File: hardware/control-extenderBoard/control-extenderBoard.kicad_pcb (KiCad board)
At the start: 4 copper layers, 197.5 x 108.9 mm, 164 parts, among them J1 12V + GND (TP), J10 SCL1 + GND (TP), J11 SDA1 + GND (TP), J12 3V3 + GND (TP), J13 12V + GND (TP), J14 SCL6 + GND (TP), J15 SDA6 + GND (TP), J16 12V + GND (TP), J17 24V IN, J18 GND, J19 3V3 + GND (TP), J2 CAT6-Shield, J20 SCL6 + GND (TP), J21 SDA6 + GND (TP), J22 SDA, SCL - ESP32, J23 I2C7 Reserve SCL/GND, J24 I2C6 Reserve SDA/GND, J25 I2C7 Reserve SDA/GND, J26 I2C6 Reserve SCL/GND, J27 CAT6-Shield, J28 CAT6-Shield, J29 Chassis, J3 Conn_01x02_Pin, J30 RX DIR, J31 TX, GND, J32 12V out, J33 5V out, J34 3V3 out, J35 Conn_01x02_Pin, J36 Conn_01x02_Pin, J37 Conn_01x02_Pin, J38 Conn_01x02_Pin, J39 Conn_01x02_Pin, J4 3V3 + GND (TP), J5 GND, J8 RS485, U1 MAX3485, U10 LM2576T-12, U13 AS5600_Breakout, U14 PCA9600D, U2 PCA9600D, U3 TCA9548A_1-to-8_I2C_Multiplex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, U4 LM2576T-3.3, U8 PCA9600D, U9 LM2576T-5

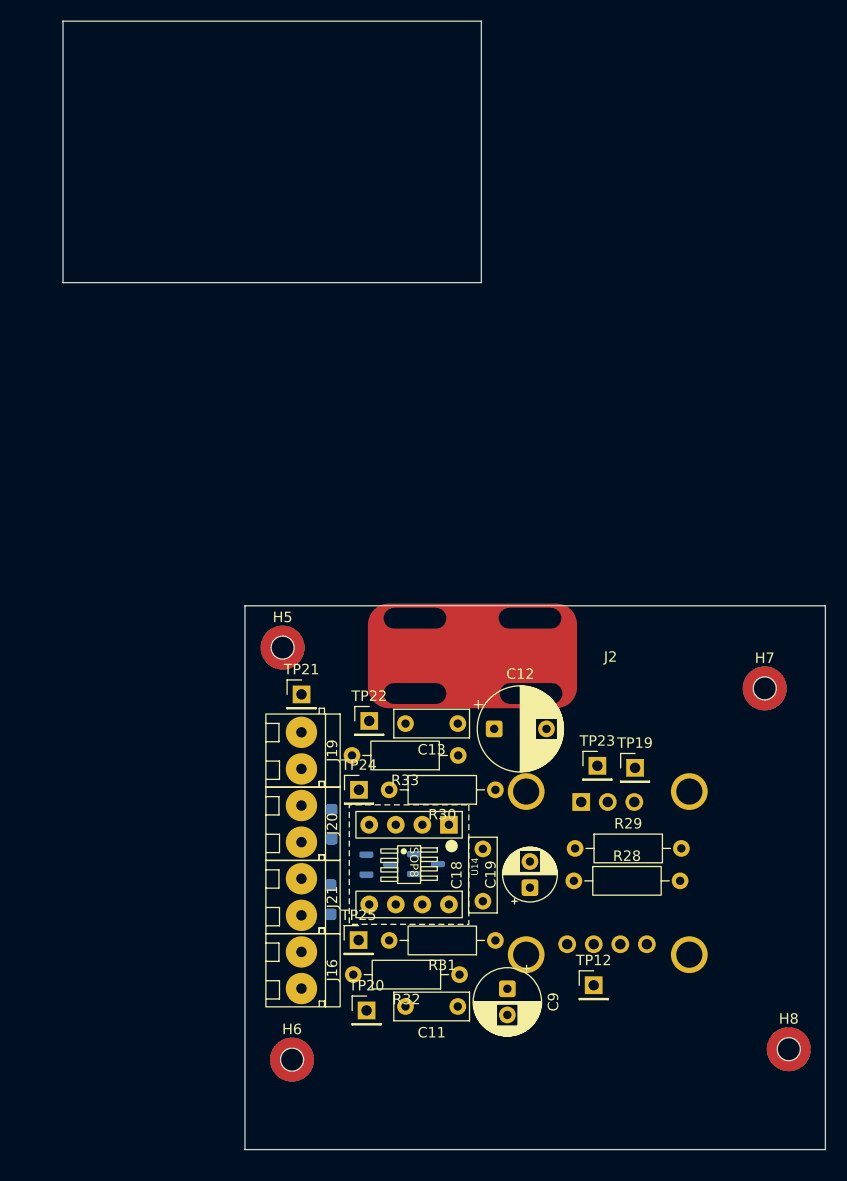
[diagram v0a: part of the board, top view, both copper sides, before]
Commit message: extenderBoard: Route separate remote/sensor-board
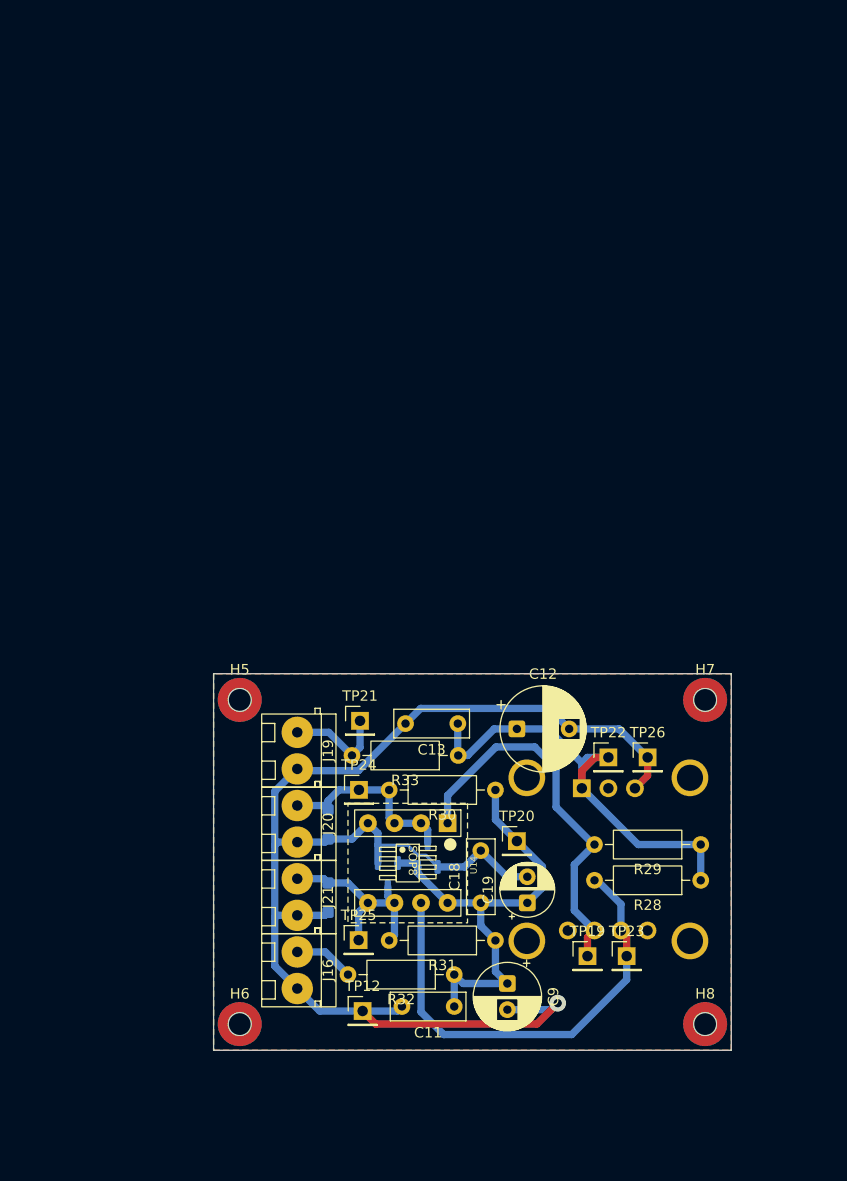
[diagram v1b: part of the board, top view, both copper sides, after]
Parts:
- removed J2: CAT6-Shield, misc_libJonny:Shield_Landing_Pad_6mmCable_ZipTie
- added TP26: GND, Connector_PinHeader_2.54mm:PinHeader_1x01_P2.54mm_Vertical, F.Cu at (225.5, 91.5)
- moved TP22 23.1 mm to (221.8, 91.5)
- moved TP12 22.2 mm to (198.2, 115.8)
- moved TP20 21.7 mm to (213.0, 99.5)
- moved TP19 18.6 mm to (219.8, 110.5)
- moved TP23 18.4 mm to (223.5, 110.5)
- moved R28 12.1 mm to (230.6, 103.2), turned to 180 degrees
- moved R29 12.0 mm to (230.6, 99.8), turned to 180 degrees
- moved H8 8.35 mm to (231.0, 117.0)
- moved H5 6.47 mm to (186.5, 86.0)
- moved TP21 6.14 mm to (198.0, 88.0)
- moved H6 6.05 mm to (186.5, 117.0)
- moved H7 5.81 mm to (231.0, 86.0)
- moved C12 2.17 mm to (213.0, 88.8)
- moved C19 1.48 mm to (214.0, 105.4)
- moved D14 1.34 mm to (200.7, 102.7), turned to -90 degrees
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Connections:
- net Net-(U13-SCL) renamed /Remote-I2C-Sensor-Board/SCL_AS5600
- net Net-(U13-SDA) renamed /Remote-I2C-Sensor-Board/SDA_AS5600
- J20 pad 1: GND_REMOTE -> /Remote-I2C-Sensor-Board/SCL_REMOTE-IN
- J20 pad 2: /Remote-I2C-Sensor-Board/SCL_REMOTE-IN -> GND_REMOTE
- J21 pad 1: GND_REMOTE -> /Remote-I2C-Sensor-Board/SDA_REMOTE-IN
- J21 pad 2: /Remote-I2C-Sensor-Board/SDA_REMOTE-IN -> GND_REMOTE
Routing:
- net GND_REMOTE: track 0.00 -> 136.5 mm, vias 0 -> 1
- net +12V_REMOTE: track 0.00 -> 44.8 mm
- net +3V3_REMOTE: track 0.00 -> 44.2 mm
- net /Remote-I2C-Sensor-Board/SDA_AS5600: track 0.00 -> 44.1 mm
- net /Remote-I2C-Sensor-Board/SCL_AS5600: track 0.00 -> 37.2 mm
- net /Remote-I2C-Sensor-Board/SDA_REMOTE-IN: track 0.00 -> 19.8 mm
- net /Remote-I2C-Sensor-Board/SCL_REMOTE-IN: track 0.00 -> 18.3 mm
- net /Remote-I2C-Sensor-Board/3V3_REMOTE-IN: track 0.00 -> 9.78 mm
- net /Remote-I2C-Sensor-Board/12V_REMOTE-IN: track 0.00 -> 5.75 mm
- added copper zone on B.Cu, net GND_REMOTE
- added copper zone on F.Cu, net GND_REMOTE
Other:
- board size 197.5 x 108.9 mm -> 188.5 x 100 mm
- board text added: "SCL"
- board text added: "SDA"

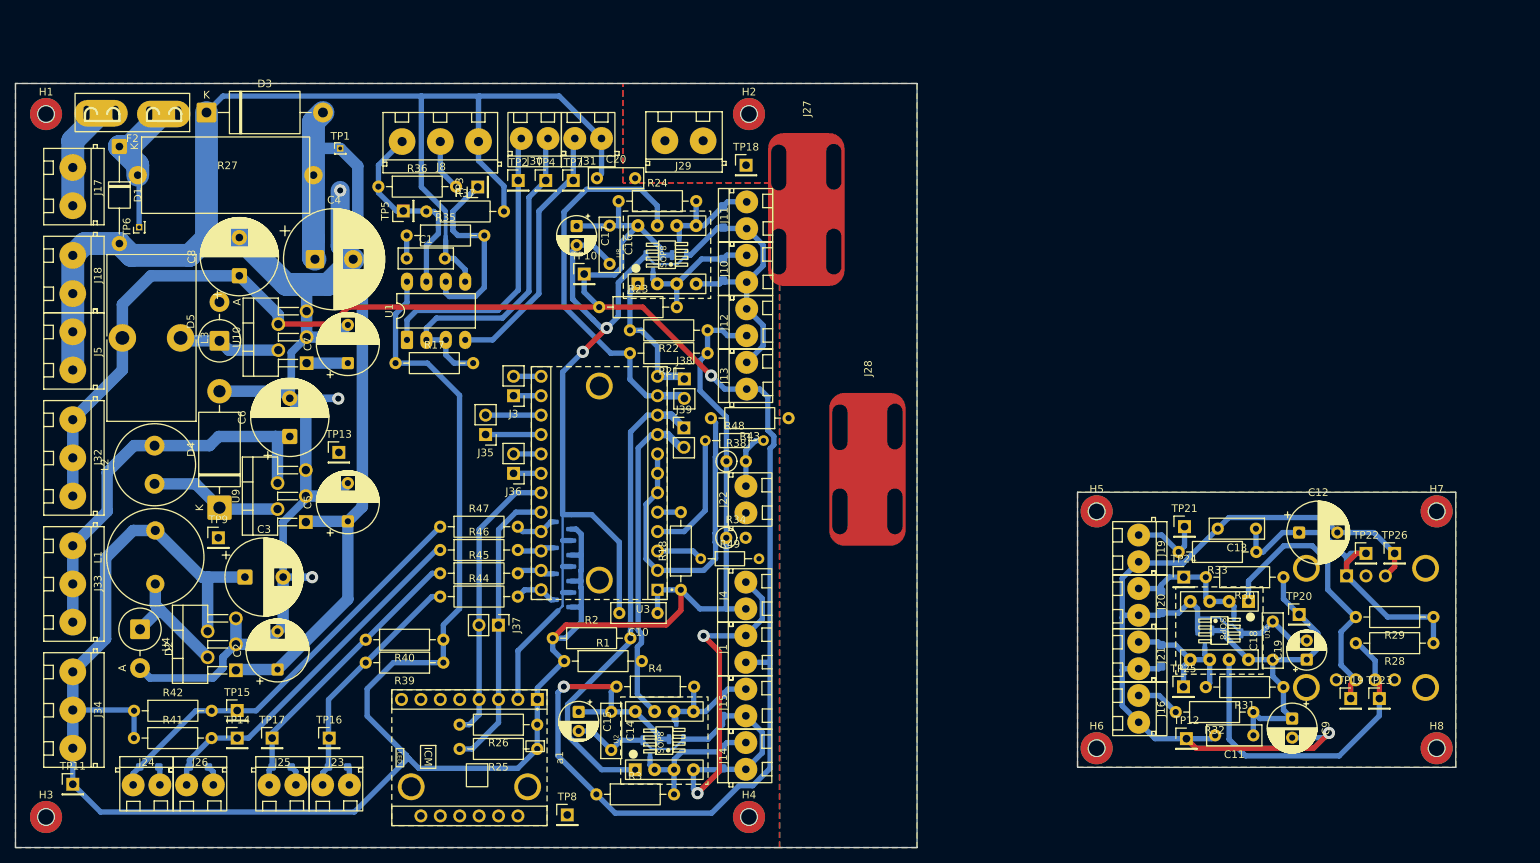
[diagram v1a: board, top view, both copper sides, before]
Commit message: extenderBoard: Add ferrite-beads, Swap 12V TVS diodes
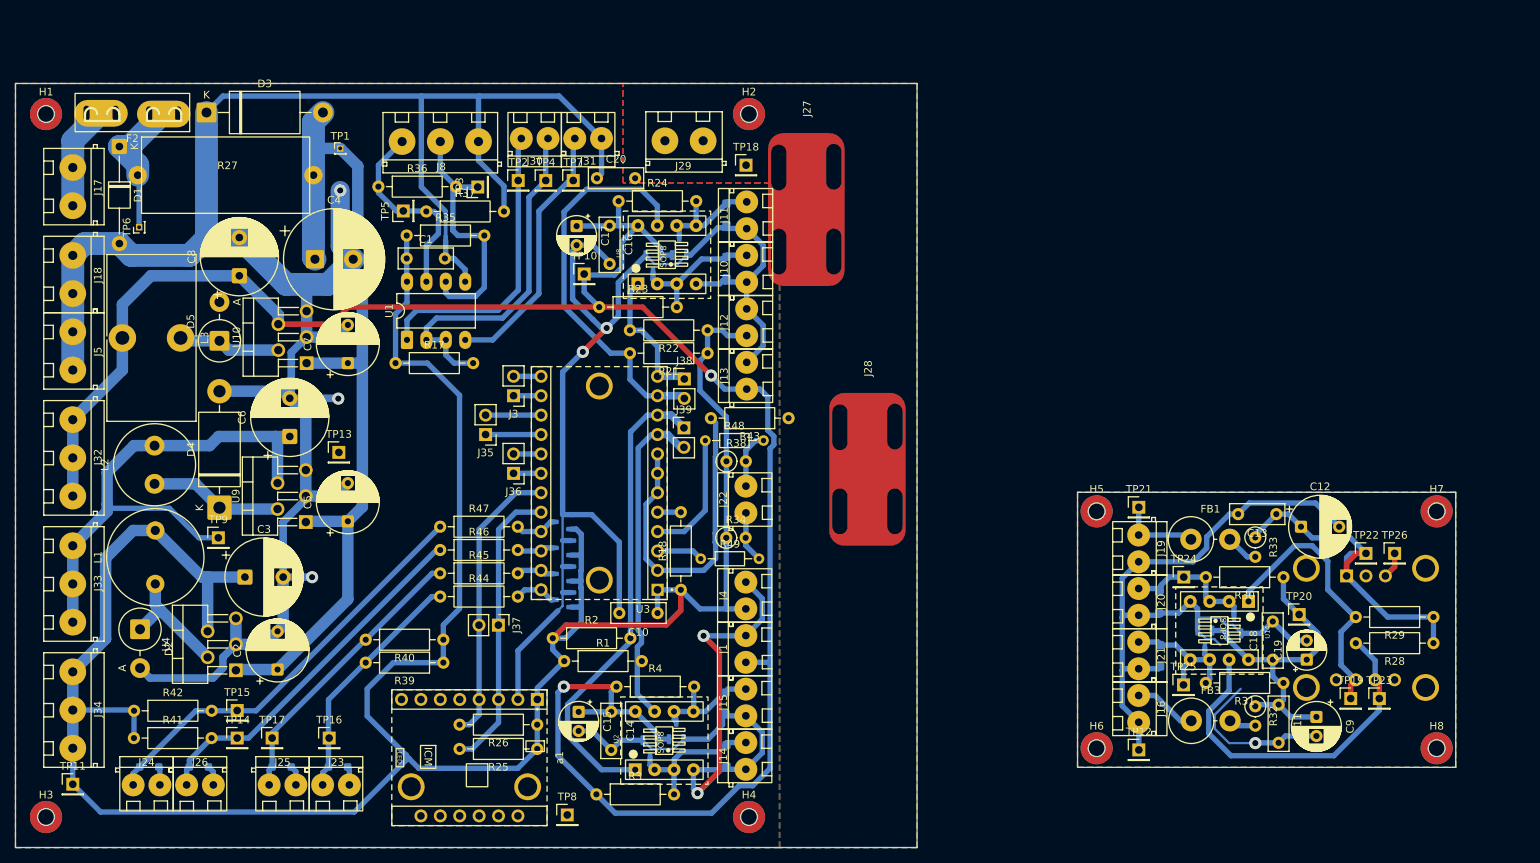
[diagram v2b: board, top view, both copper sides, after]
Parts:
- removed D15: SMF12VTR, Diode_SMD:D_SOD-123F
- added D31: PESD12VL1BA, Diode_SMD:D_SOD-123F, B.Cu at (138.0, 54.1)
- added FB1: FerriteBead AWBC-09, Resistor_THT:R_Axial_DIN0614_L14.3mm_D5.7mm_P5.08mm_Vertical, F.Cu at (198.8, 89.7)
- added FB3: FerriteBead AWBC-09, Resistor_THT:R_Axial_DIN0614_L14.3mm_D5.7mm_P5.08mm_Vertical, F.Cu at (198.9, 113.4)
- D11, D12, D16, D8, D9: value SMF12VTR -> PESD12VL1BA
- R32, R33: footprint Resistor_THT:R_Axial_DIN0207_L6.3mm_D2.5mm_P10.16mm_Horizontal -> Resistor_THT:R_Axial_DIN0207_L6.3mm_D2.5mm_P2.54mm_Vertical
- moved D9 70.5 mm to (138.0, 118.0), turned to 90 degrees
- moved D12 58.8 mm to (194.8, 104.9), turned to 90 degrees
- moved D8 7.27 mm to (138.0, 47.1), turned to 90 degrees
- moved D16 6.99 mm to (194.7, 97.9), turned to 90 degrees
- moved TP21 6.49 mm to (192.0, 85.5)
- moved TP12 6.40 mm to (192.0, 117.2)
- moved C11 5.21 mm to (210.3, 111.3), turned to -90 degrees
- moved C13 3.28 mm to (210.0, 86.4)
- moved C9 3.18 mm to (215.3, 112.9)
- moved R33 1.91 mm to (207.3, 89.4), turned to -90 degrees
- moved R32 0.80 mm to (207.3, 111.5), turned to -90 degrees
- moved C12 0.80 mm to (213.2, 88.0)
- moved R31 0.54 mm to (210.9, 108.5)
- moved D11 0.46 mm to (137.9, 111.1), turned to 90 degrees
- moved TP25 0.25 mm to (197.9, 108.7)
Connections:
- D11 pad 1: /SDA_Boost1 -> GND
- D11 pad 2: GND -> /SDA_Boost1
- D12 pad 1: /SCL_Boost1 -> GND_REMOTE
- D12 pad 2: GND -> /Remote-I2C-Sensor-Board/SDA_REMOTE-IN
- D16 pad 1: /Remote-I2C-Sensor-Board/SDA_REMOTE-IN -> GND_REMOTE
- D16 pad 2: GND_REMOTE -> /Remote-I2C-Sensor-Board/SCL_REMOTE-IN
- D8 pad 1: /SCL_Boost2 -> GND
- D8 pad 2: GND -> /SDA_Boost2
- D9 pad 1: /SDA_Boost2 -> GND
- D9 pad 2: GND -> /SCL_Boost1
- R32 pad 2: /Remote-I2C-Sensor-Board/12V_REMOTE-IN -> Net-(FB3-Pad2)
- R33 pad 2: /Remote-I2C-Sensor-Board/3V3_REMOTE-IN -> Net-(FB1-Pad2)
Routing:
- net +5V: track 53.5 -> 69.9 mm
- net GND_REMOTE: track 136.5 -> 122.4 mm
- net /ESP32_SDA: track 0.00 -> 6.74 mm
- net Net-(FB1-Pad2): track 0.00 -> 4.29 mm
- net Net-(FB3-Pad2): track 0.00 -> 3.57 mm
- net +3V3: track 341.5 -> 344.5 mm
- net /Remote-I2C-Sensor-Board/SDA_AS5600: track 44.1 -> 47.0 mm
- net /Remote-I2C-Sensor-Board/12V_REMOTE-IN: track 5.75 -> 8.25 mm
- net +24V filtered: track 114.8 -> 116.8 mm
- net /RS485-A: track 32.2 -> 33.9 mm
- net +12V_REMOTE: track 44.8 -> 43.4 mm
- net /Remote-I2C-Sensor-Board/3V3_REMOTE-IN: track 9.78 -> 10.7 mm
- net /Remote-I2C-Sensor-Board/SCL_AS5600: track 37.2 -> 36.4 mm
- net /Remote-I2C-Sensor-Board/SDA_REMOTE-IN: track 19.8 -> 19.0 mm
- net +3V3_REMOTE: track 44.2 -> 45.0 mm

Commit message: extenderBoard: Optimize zones, routing, Fix errors - DRC pass
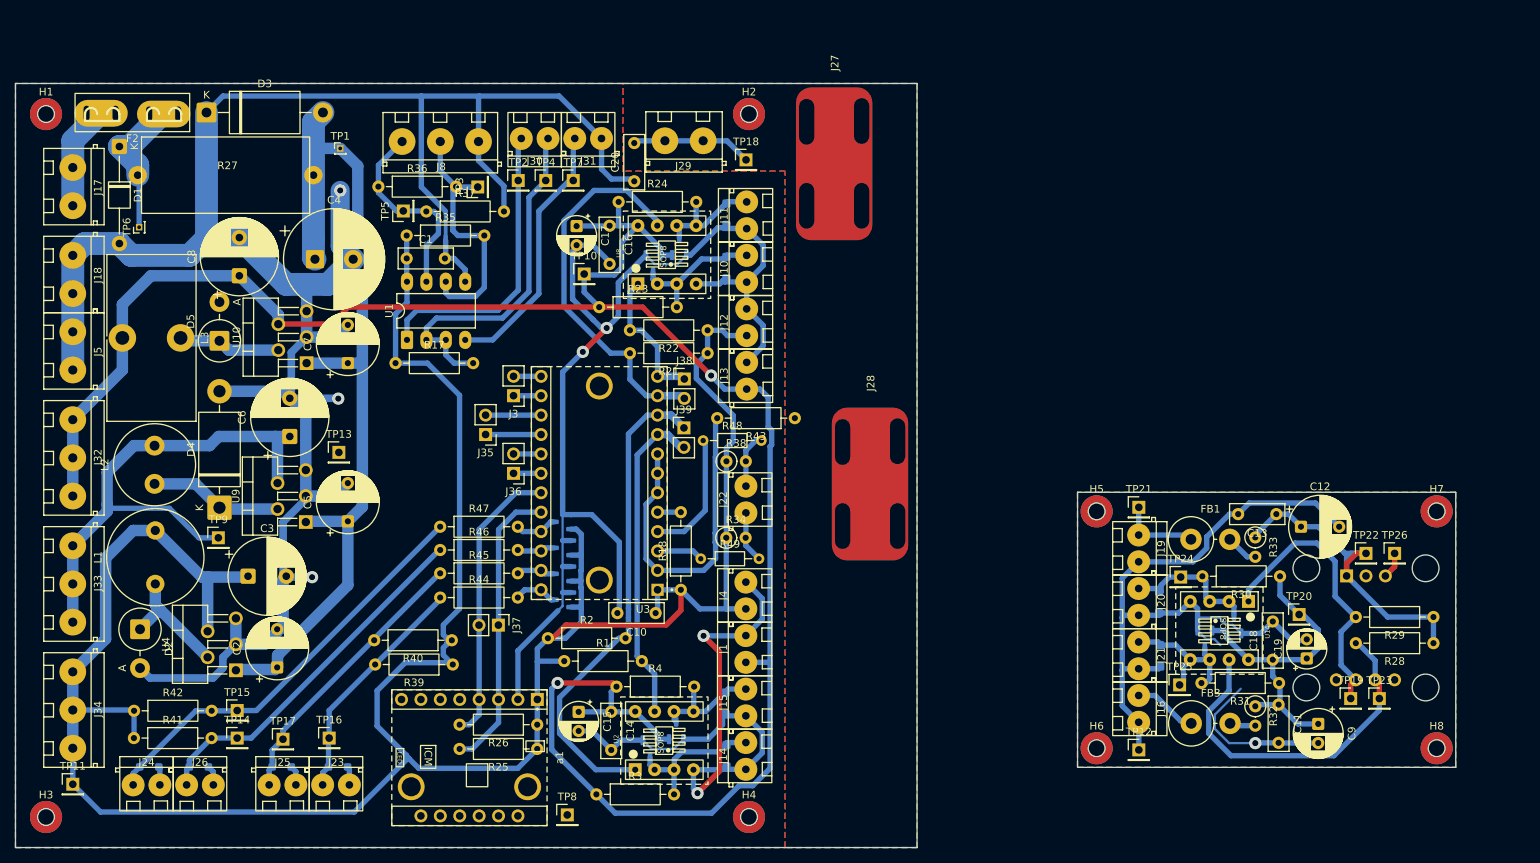
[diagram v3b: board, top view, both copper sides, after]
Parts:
- moved J27 7.01 mm to (152.1, 40.5)
- moved C20 4.90 mm to (126.0, 42.8), turned to 90 degrees
- moved J28 1.95 mm to (156.8, 82.4)
- moved TP17 1.43 mm to (80.0, 115.8)
- moved R39 1.26 mm to (102.2, 106.0)
- moved R40 1.11 mm to (102.1, 102.9)
- moved C9 0.94 mm to (215.5, 113.8)
- moved R43 0.82 mm to (147.0, 73.8)
- moved TP18 0.69 mm to (140.6, 40.0)
- moved R2 0.64 mm to (114.7, 102.6)
- moved R31 0.57 mm to (210.4, 108.5)
- moved TP25 0.51 mm to (197.4, 108.7)
- moved R30 0.46 mm to (210.5, 94.5)
- moved C3 0.42 mm to (75.4, 94.5)
- moved TP24 0.40 mm to (197.5, 94.6)
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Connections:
- H2 pad 1: GND -> Chassis
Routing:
- net Chassis: track 0.00 -> 15.8 mm
- net +3V3: track 344.5 -> 350.7 mm
- net GND: track 579.4 -> 583.0 mm
- net /I2C1_SDA: track 52.0 -> 50.1 mm
- net /I2C0_SCL: track 62.5 -> 64.3 mm
- net +12V: track 277.1 -> 278.6 mm
- net /Remote-I2C-Sensor-Board/SCL_AS5600: track 36.4 -> 37.3 mm
- net Net-(D18-A1): track 31.7 -> 30.9 mm
- net /I2C0_SDA: track 43.2 -> 42.4 mm
- net /Remote-I2C-Sensor-Board/SDA_REMOTE-IN: track 19.0 -> 19.8 mm
- net +12V_REMOTE: track 43.4 -> 43.9 mm
- net Net-(D6-A1): track 37.6 -> 37.1 mm
